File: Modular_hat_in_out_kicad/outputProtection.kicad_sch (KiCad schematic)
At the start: 2 parts

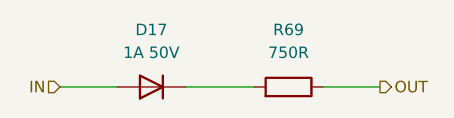
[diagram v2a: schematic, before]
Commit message: [ADD] Footprints
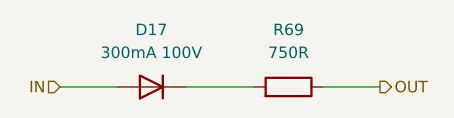
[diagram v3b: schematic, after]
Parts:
- D17: value 1A 50V -> 300mA 100V; footprint (none) -> Modular Shield:D_0603_1608Metric; LCSC C727079 -> C727112
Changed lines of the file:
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@@
 			)
 		)
-		(property "Value" "1A 50V"
+		(property "Value" "300mA 100V"
 			(at 55.88 30.48 0)
 			(effects
@@
 			)
 		)
-		(property "Footprint" ""
+		(property "Footprint" "Modular Shield:D_0603_1608Metric"
 			(at 55.88 34.29 0)
 			(effects
@@
 			)
 		)
-		(property "LCSC" "C727079"
+		(property "LCSC" "C727112"
 			(at 55.88 34.29 0)
 			(effects

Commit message: [ADD] Revision number (1.0)
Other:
- title: (none) -> Output Protection
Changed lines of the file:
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@@
 	(generator_version "8.0")
 	(paper "User" 132.004 99.9998)
+	(title_block
+		(title "Output Protection")
+		(date "2024-08-21")
+		(rev "1.0")
+	)
 	(wire
 		(pts
